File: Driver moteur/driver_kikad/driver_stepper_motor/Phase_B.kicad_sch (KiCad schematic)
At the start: 19 parts

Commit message: Driver modifié avec les bonnes valeurs et les bonnes datasheet
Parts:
- added RB5, RB6: 100k, Resistor_SMD:R_0603_1608Metric, symbol Device:R_Small
- RB_shunt1: value à déterminer -> 0,75m
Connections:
- net 24V: no longer CB1.2, Isens_B1.3 (Vs)
- net GND: now also RB5.2; no longer Isens_B1.1 (REF)
- new net: Isens_B1.1 (REF), RB5.1, RB6.2
- new net 3,3V: CB1.2, Isens_B1.3 (Vs), RB6.1
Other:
- note added: "Voutmax=3V Iloadmax=10A Vref=Vs/2"
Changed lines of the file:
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@@
     (company "Tom CHARBONNEAU")
   )
-  (junction (at 146.05 43.18) (diameter 0) (color 0 0 0 0)
-  )
   (junction (at 163.83 97.79) (diameter 0) (color 0 0 0 0)
   )
@@
   (junction (at 146.05 60.96) (diameter 0) (color 0 0 0 0)
   )
+  (junction (at 114.3 44.45) (diameter 0) (color 0 0 0 0)
+  )
+  (junction (at 87.63 44.45) (diameter 0) (color 0 0 0 0)
+  )
   (junction (at 128.27 97.79) (diameter 0) (color 0 0 0 0)
   )
+  (junction (at 87.63 58.42) (diameter 0) (color 0 0 0 0)
+  )
   (junction (at 146.05 71.12) (diameter 0) (color 0 0 0 0)
   )
   (junction (at 146.05 55.88) (diameter 0) (color 0 0 0 0)
   )
-  (junction (at 114.3 43.18) (diameter 0) (color 0 0 0 0)
-  )
   (junction (at 86.36 88.9) (diameter 0) (color 0 0 0 0)
   )
@@
     (stroke (width 0) (type default) (color 0 0 0 0))
   )
-  (wire (pts (xy 146.05 43.18) (xy 146.05 55.88))
-    (stroke (width 0) (type default) (color 0 0 0 0))
-  )
   (wire (pts (xy 58.42 91.44) (xy 58.42 109.22))
     (stroke (width 0) (type default) (color 0 0 0 0))
@@
     (stroke (width 0) (type default) (color 0 0 0 0))
   )
+  (wire (pts (xy 87.63 58.42) (xy 101.6 58.42))
+    (stroke (width 0) (type default) (color 0 0 0 0))
+  )
   (wire (pts (xy 86.36 81.28) (xy 86.36 80.01))
     (stroke (width 0) (type default) (color 0 0 0 0))
@@
     (stroke (width 0) (type default) (color 0 0 0 0))
   )
+  (wire (pts (xy 87.63 64.77) (xy 87.63 67.31))
+    (stroke (width 0) (type default) (color 0 0 0 0))
+  )
   (wire (pts (xy 228.6 86.36) (xy 228.6 80.01))
     (stroke (width 0) (type default) (color 0 0 0 0))
   )
+  (wire (pts (xy 85.09 44.45) (xy 87.63 44.45))
+    (stroke (width 0) (type default) (color 0 0 0 0))
+  )
   (wire (pts (xy 153.67 97.79) (xy 163.83 97.79))
     (stroke (width 0) (type default) (color 0 0 0 0))
@@
     (stroke (width 0) (type default) (color 0 0 0 0))
   )
+  (wire (pts (xy 114.3 44.45) (xy 114.3 48.26))
+    (stroke (width 0) (type default) (color 0 0 0 0))
+  )
   (wire (pts (xy 228.6 91.44) (xy 228.6 109.22))
     (stroke (width 0) (type default) (color 0 0 0 0))
@@
     (stroke (width 0) (type default) (color 0 0 0 0))
   )
+  (wire (pts (xy 87.63 44.45) (xy 87.63 52.07))
+    (stroke (width 0) (type default) (color 0 0 0 0))
+  )
   (wire (pts (xy 115.57 83.82) (xy 120.65 83.82))
     (stroke (width 0) (type default) (color 0 0 0 0))
@@
     (stroke (width 0) (type default) (color 0 0 0 0))
   )
+  (wire (pts (xy 87.63 44.45) (xy 114.3 44.45))
+    (stroke (width 0) (type default) (color 0 0 0 0))
+  )
   (wire (pts (xy 80.01 104.14) (xy 99.06 104.14))
     (stroke (width 0) (type default) (color 0 0 0 0))
@@
     (stroke (width 0) (type default) (color 0 0 0 0))
   )
-  (wire (pts (xy 146.05 40.64) (xy 146.05 43.18))
+  (wire (pts (xy 87.63 58.42) (xy 87.63 59.69))
+    (stroke (width 0) (type default) (color 0 0 0 0))
+  )
+  (wire (pts (xy 146.05 52.07) (xy 146.05 55.88))
     (stroke (width 0) (type default) (color 0 0 0 0))
   )
@@
     (stroke (width 0) (type default) (color 0 0 0 0))
   )
+  (wire (pts (xy 87.63 57.15) (xy 87.63 58.42))
+    (stroke (width 0) (type default) (color 0 0 0 0))
+  )
   (wire (pts (xy 128.27 97.79) (xy 139.7 97.79))
     (stroke (width 0) (type default) (color 0 0 0 0))
@@
     (stroke (width 0) (type default) (color 0 0 0 0))
   )
-  (wire (pts (xy 114.3 43.18) (xy 114.3 48.26))
-    (stroke (width 0) (type default) (color 0 0 0 0))
-  )
   (wire (pts (xy 190.5 97.79) (xy 190.5 101.6))
     (stroke (width 0) (type default) (color 0 0 0 0))
@@
     (stroke (width 0) (type default) (color 0 0 0 0))
   )
-  (wire (pts (xy 114.3 43.18) (xy 146.05 43.18))
-    (stroke (width 0) (type default) (color 0 0 0 0))
-  )
   (wire (pts (xy 124.46 55.88) (xy 146.05 55.88))
     (stroke (width 0) (type default) (color 0 0 0 0))
   )
-  (wire (pts (xy 114.3 41.91) (xy 114.3 43.18))
+  (wire (pts (xy 114.3 41.91) (xy 114.3 44.45))
     (stroke (width 0) (type default) (color 0 0 0 0))
   )
@@
   )
   (text "Vout = (Iload x Rshunt) x Gain + Vref" (at 127 66.04 0)
+    (effects (font (size 1.27 1.27)) (justify left bottom))
+  )
+  (text "Voutmax=3V\nIloadmax=10A\nVref=Vs/2" (at 163.83 60.96 0)
     (effects (font (size 1.27 1.27)) (justify left bottom))
   )
@@
     (effects (font (size 1.27 1.27)) (justify left bottom))
   )
-  (hierarchical_label "24V" (shape input) (at 146.05 40.64 90)
+  (hierarchical_label "3,3V" (shape input) (at 85.09 44.45 180)
+    (effects (font (size 1.27 1.27)) (justify right))
+  )
+  (hierarchical_label "24V" (shape input) (at 146.05 52.07 90)
     (effects (font (size 1.27 1.27)) (justify left))
   )
@@
     (pin "2")
   )
-  (symbol (lib_id "power:GND") (at 101.6 58.42 270) (unit 1)
-    (in_bom yes) (on_board yes)
-    (property "Reference" "#PWR0111" (id 0) (at 95.25 58.42 0)
-      (effects (font (size 1.27 1.27)) hide)
-    )
-    (property "Value" "GND" (id 1) (at 97.79 60.96 90)
-      (effects (font (size 1.27 1.27)) (justify left))
-    )
-    (property "Footprint" "" (id 2) (at 101.6 58.42 0)
-      (effects (font (size 1.27 1.27)) hide)
-    )
-    (property "Datasheet" "" (id 3) (at 101.6 58.42 0)
-      (effects (font (size 1.27 1.27)) hide)
-    )
-    (pin "1")
-  )
   (symbol (lib_id "Transistor_FET:FDC2512") (at 125.73 83.82 0) (unit 1)
     (in_bom yes) (on_board yes) (fields_autoplaced)
@@
       (effects (font (size 1.27 1.27)) (justify left))
     )
-    (property "Value" "à déterminer" (id 1) (at 148.59 59.6899 0)
+    (property "Value" "0,75m" (id 1) (at 148.59 59.6899 0)
       (effects (font (size 1.27 1.27)) (justify left))
     )
@@
     (pin "6")
   )
+  (symbol (lib_id "power:GND") (at 87.63 67.31 0) (unit 1)
+    (in_bom yes) (on_board yes)
+    (property "Reference" "#PWR?" (id 0) (at 87.63 73.66 0)
+      (effects (font (size 1.27 1.27)) hide)
+    )
+    (property "Value" "GND" (id 1) (at 87.63 71.12 0))
+    (property "Footprint" "" (id 2) (at 87.63 67.31 0)
+      (effects (font (size 1.27 1.27)) hide)
+    )
+    (property "Datasheet" "" (id 3) (at 87.63 67.31 0)
+      (effects (font (size 1.27 1.27)) hide)
+    )
+    (pin "1")
+  )
   (symbol (lib_id "Device:D_Small") (at 200.66 83.82 90) (unit 1)
     (in_bom yes) (on_board yes)
@@
     )
     (property "Datasheet" "~" (id 3) (at 200.66 83.82 90)
+      (effects (font (size 1.27 1.27)) hide)
+    )
+    (pin "1")
+    (pin "2")
+  )
+  (symbol (lib_id "Device:R_Small") (at 87.63 62.23 0) (unit 1)
+    (in_bom yes) (on_board yes)
+    (property "Reference" "RB5" (id 0) (at 85.09 62.23 90))
+    (property "Value" "100k" (id 1) (at 90.17 62.23 90))
+    (property "Footprint" "Resistor_SMD:R_0603_1608Metric" (id 2) (at 87.63 62.23 0)
+      (effects (font (size 1.27 1.27)) hide)
+    )
+    (property "Datasheet" "~" (id 3) (at 87.63 62.23 0)
       (effects (font (size 1.27 1.27)) hide)
     )
@@
     (pin "6")
   )
+  (symbol (lib_id "Device:R_Small") (at 87.63 54.61 0) (unit 1)
+    (in_bom yes) (on_board yes)
+    (property "Reference" "RB6" (id 0) (at 85.09 54.61 90))
+    (property "Value" "100k" (id 1) (at 90.17 54.61 90))
+    (property "Footprint" "Resistor_SMD:R_0603_1608Metric" (id 2) (at 87.63 54.61 0)
+      (effects (font (size 1.27 1.27)) hide)
+    )
+    (property "Datasheet" "~" (id 3) (at 87.63 54.61 0)
+      (effects (font (size 1.27 1.27)) hide)
+    )
+    (pin "1")
+    (pin "2")
+  )
   (symbol (lib_id "Transistor_FET:FDC2512") (at 125.73 109.22 0) (unit 1)

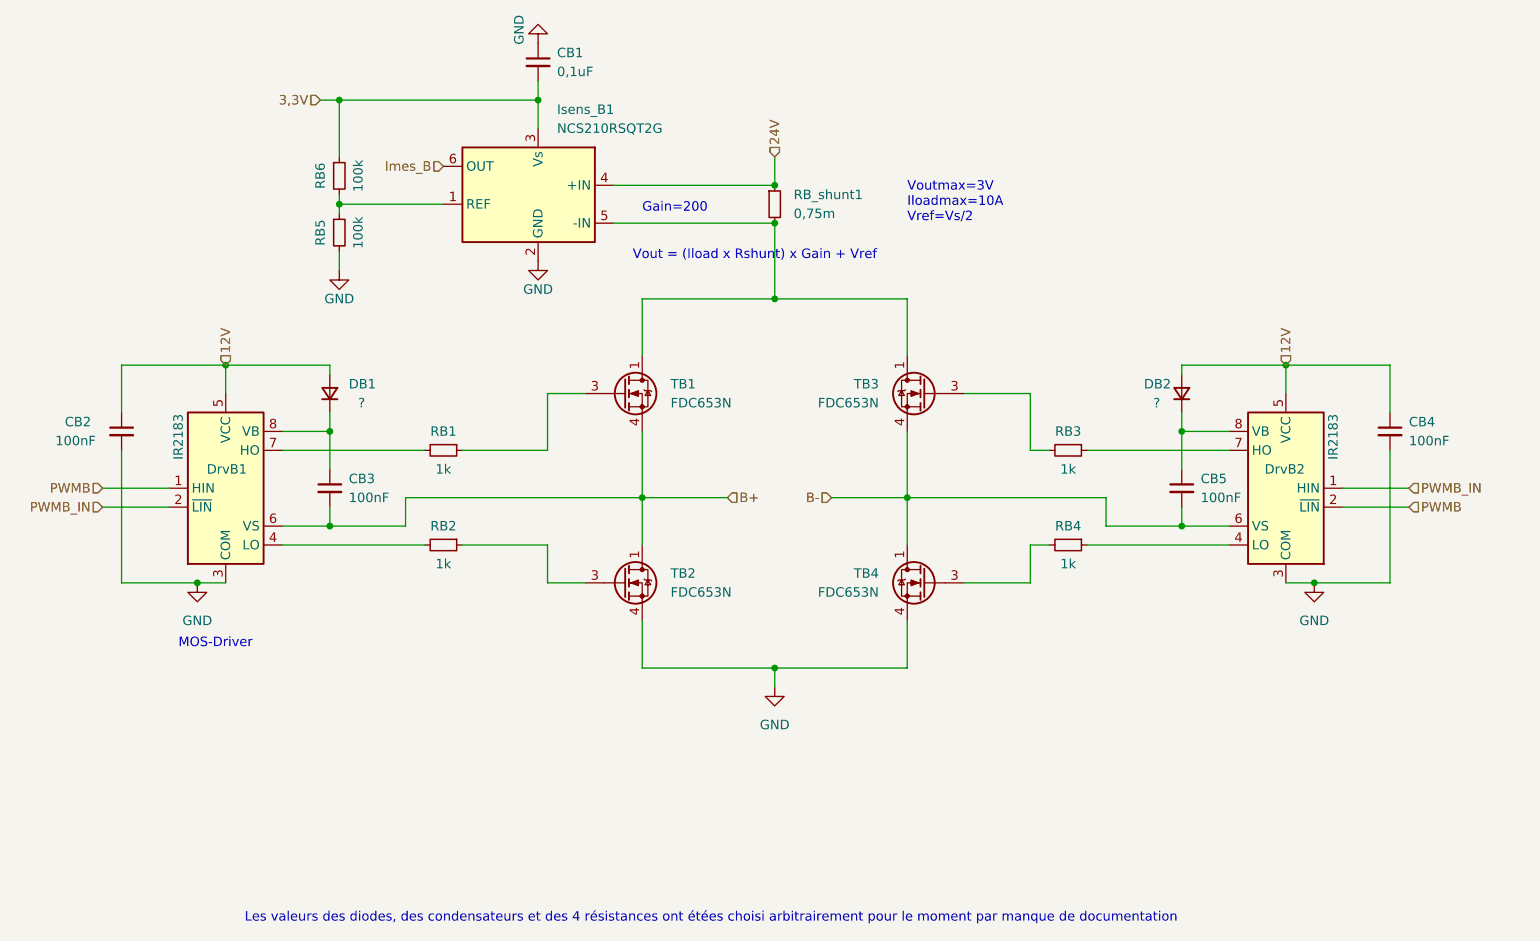
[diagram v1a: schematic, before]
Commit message: PCB root sans erreurs
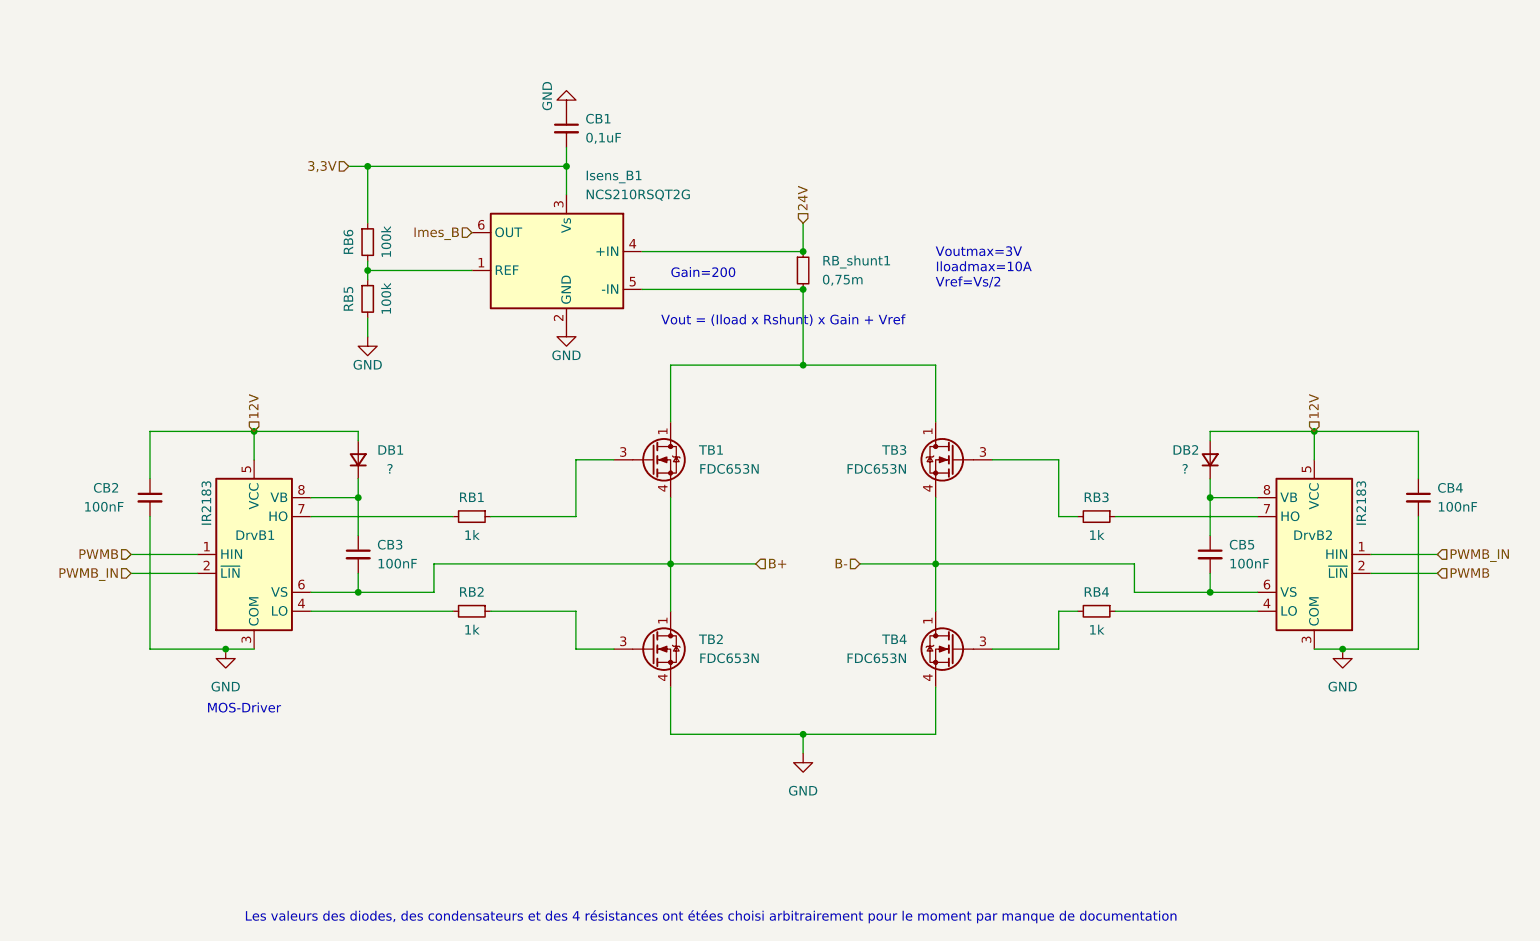
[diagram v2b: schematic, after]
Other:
- moved on the sheet: CB1, CB2, CB3, CB4, CB5, DB1, DB2, DrvB1, DrvB2, Isens_B1, RB1, RB2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
